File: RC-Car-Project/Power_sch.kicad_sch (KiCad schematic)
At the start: 20 parts, among them U2 A6986F3V3TR

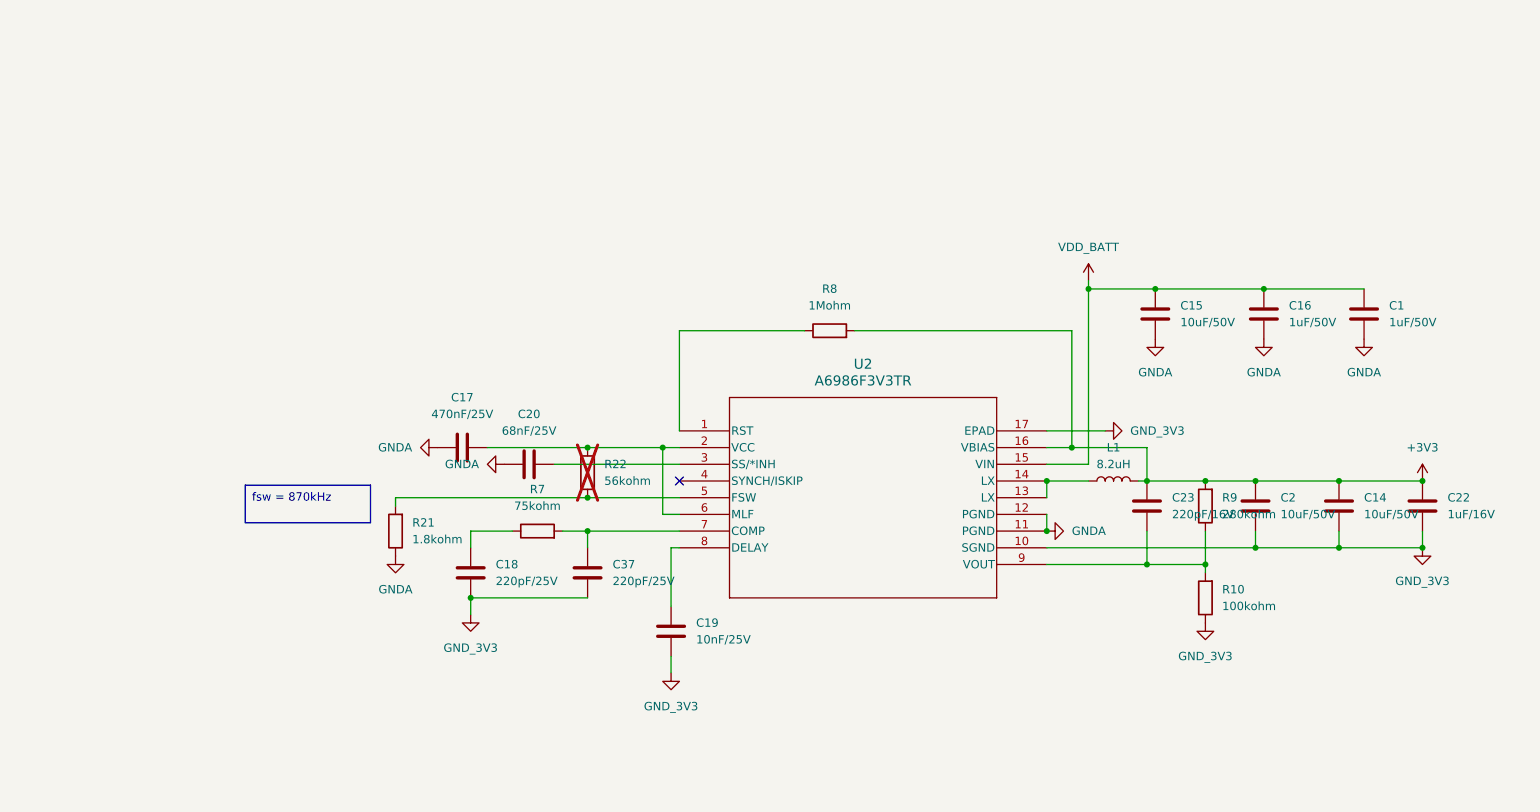
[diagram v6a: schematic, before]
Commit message: Add 12V buck
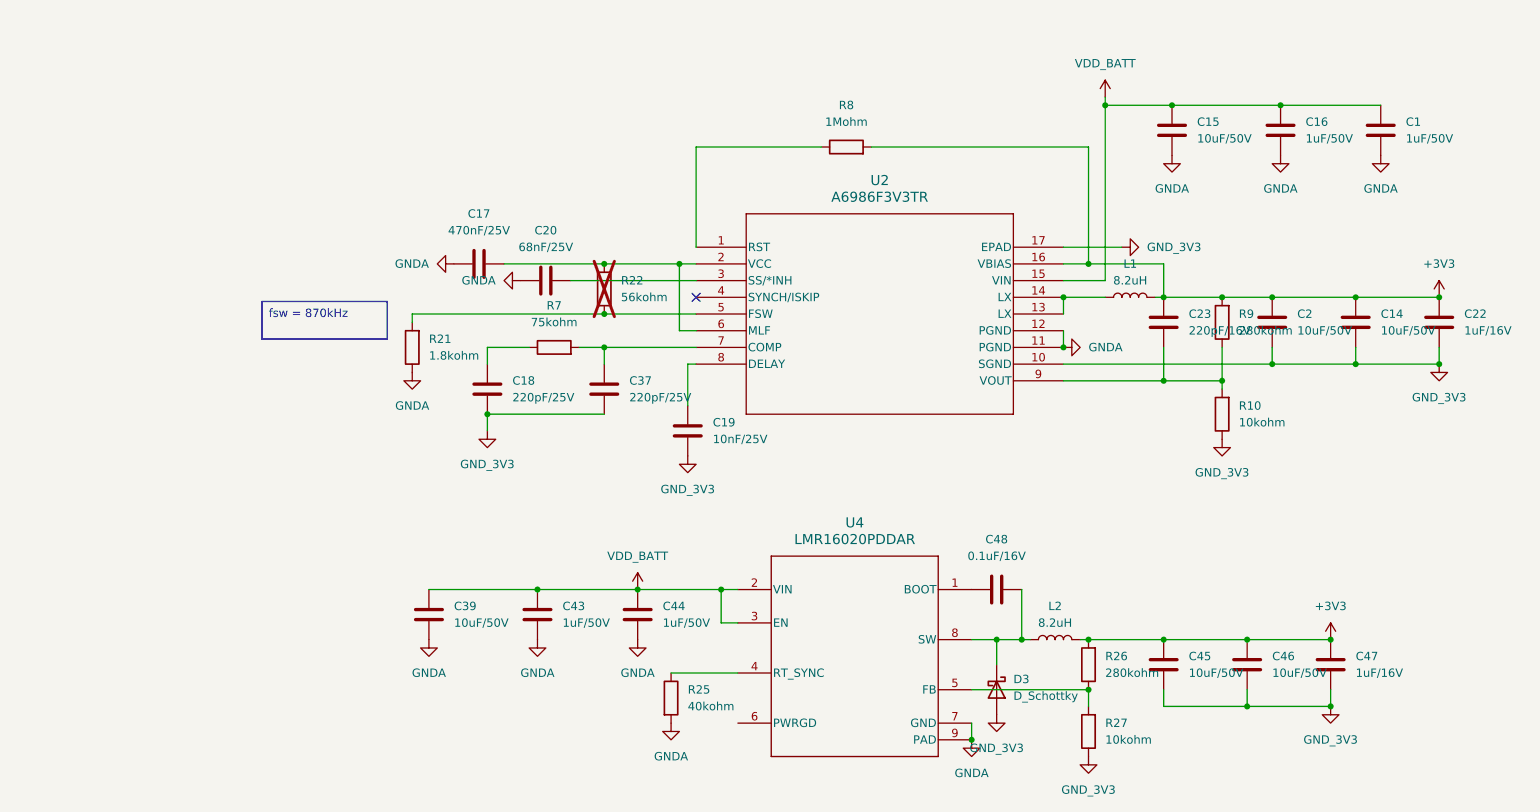
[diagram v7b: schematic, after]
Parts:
- added C39, C45, C46: 10uF/50V, Capacitor_SMD:C_1210_3225Metric, symbol Device:C
- added C43, C44: 1uF/50V, Capacitor_SMD:C_0201_0603Metric, symbol Device:C
- added C47: 1uF/16V, Capacitor_SMD:C_0201_0603Metric, symbol Device:C
- added C48: 0.1uF/16V, Capacitor_SMD:C_0201_0603Metric, symbol Device:C
- added D3: D_Schottky, Diode_SMD:Nexperia_CFP3_SOD-123W, symbol Device:D_Schottky
- added L2: 8.2uH, Inductor_SMD:L_Wuerth_MAPI-4030, symbol Device:L
- added R25: 40kohm, Resistor_SMD:R_0201_0603Metric, symbol Device:R
- added R26: 280kohm, Resistor_SMD:R_0201_0603Metric, symbol Device:R
- added R27: 10kohm, Resistor_SMD:R_0201_0603Metric, symbol Device:R
- added U4: LMR16020PDDAR, footprints:DDA0008E_N, symbol LMR16020PDDAR:LMR16020PDDAR
- R10: value 100kohm -> 10kohm
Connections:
- net +3V3: now also C45.1, C46.1, C47.1, L2.2, R26.2
- net GNDA: now also C39.2, C43.2, C44.2, R25.2, U4.7 (GND), U4.9 (PAD)
- net GND_3V3: now also C45.2, C46.2, C47.2, D3.2 (A), R27.1
- net VDD_BATT: now also C39.1, C43.1, C44.1, U4.2 (VIN), U4.3 (EN)
- new net: C48.2, U4.1 (BOOT)
- new net: R25.1, U4.4 (RT_SYNC)
- new net: R26.1, R27.2, U4.5 (FB)
- new net: C48.1, D3.1 (K), L2.1, U4.8 (SW)
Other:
- moved on the sheet: C1, C14, C15, C16, C17, C18, C19, C2, C20, C22, C23, C37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

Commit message: Added Camera Connector, Minor Controller Fixes
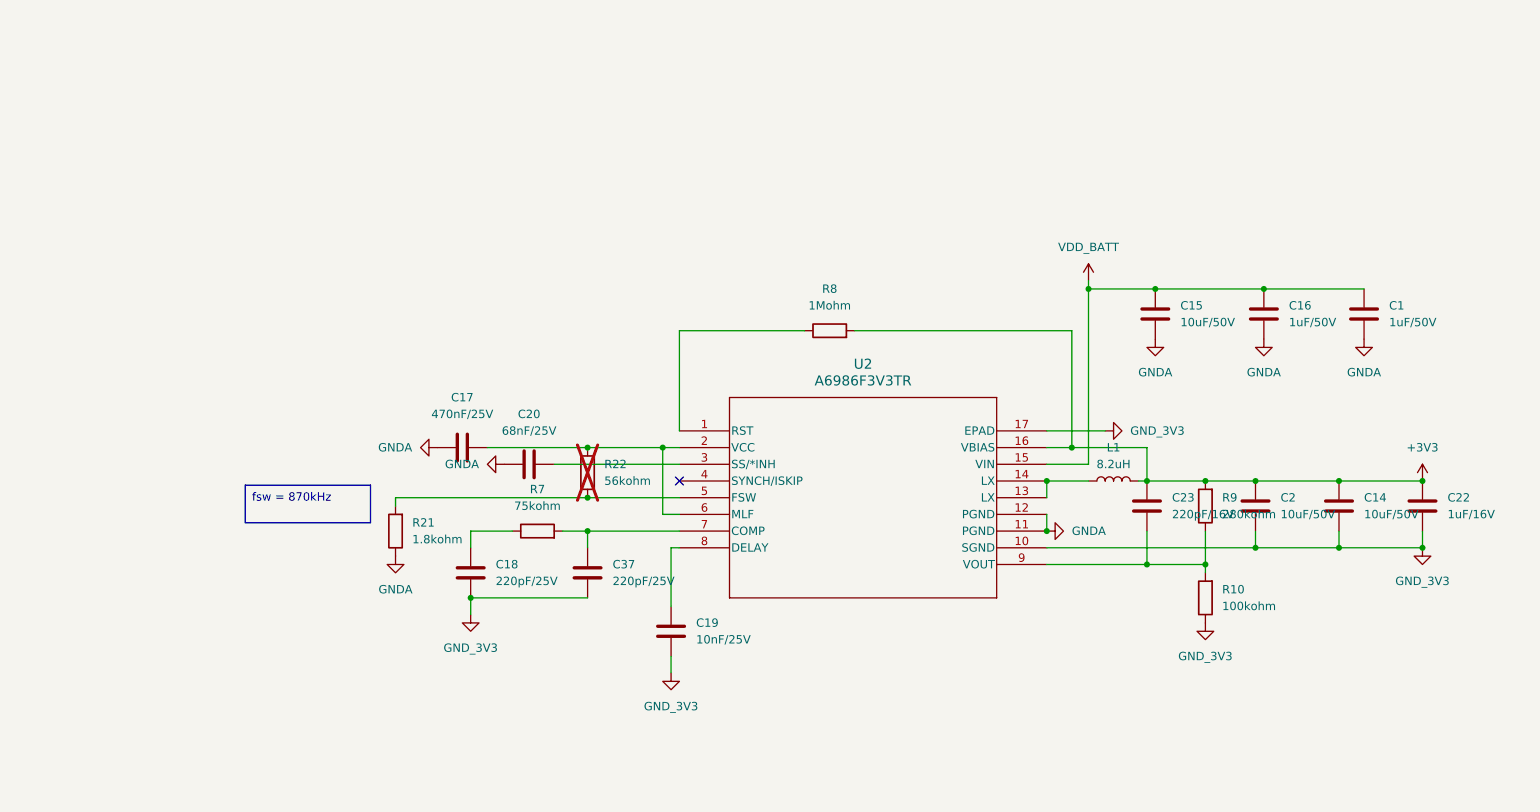
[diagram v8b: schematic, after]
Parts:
- removed C39, C45, C46: 10uF/50V, Capacitor_SMD:C_1210_3225Metric, symbol Device:C
- removed C43, C44: 1uF/50V, Capacitor_SMD:C_0201_0603Metric, symbol Device:C
- removed C47: 1uF/16V, Capacitor_SMD:C_0201_0603Metric, symbol Device:C
- removed C48: 0.1uF/16V, Capacitor_SMD:C_0201_0603Metric, symbol Device:C
- removed D3: D_Schottky, Diode_SMD:Nexperia_CFP3_SOD-123W, symbol Device:D_Schottky
- removed L2: 8.2uH, Inductor_SMD:L_Wuerth_MAPI-4030, symbol Device:L
- removed R25: 40kohm, Resistor_SMD:R_0201_0603Metric, symbol Device:R
- removed R26: 280kohm, Resistor_SMD:R_0201_0603Metric, symbol Device:R
- removed R27: 10kohm, Resistor_SMD:R_0201_0603Metric, symbol Device:R
- removed U4: LMR16020PDDAR, footprints:DDA0008E_N, symbol LMR16020PDDAR:LMR16020PDDAR
- R10: value 10kohm -> 100kohm
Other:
- moved on the sheet: C1, C14, C15, C16, C17, C18, C19, C2, C20, C22, C23, C37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
